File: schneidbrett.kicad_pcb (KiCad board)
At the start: 4 copper layers, 129 parts, among them J1 USB_C_Receptacle, J2 Audio_Jack_Input, J3 Audio_Jack_Output, J4 UART_CONNECTOR, J6 I2C_CONNECTOR, J7 ST-LINK_V2_20Pin_Connector, U1 MAX604CSA, U2 AD9833xRM, U3 STM32F767ZITx, U4 LM4881M, U5 FT230XQ, Y1 25MHz

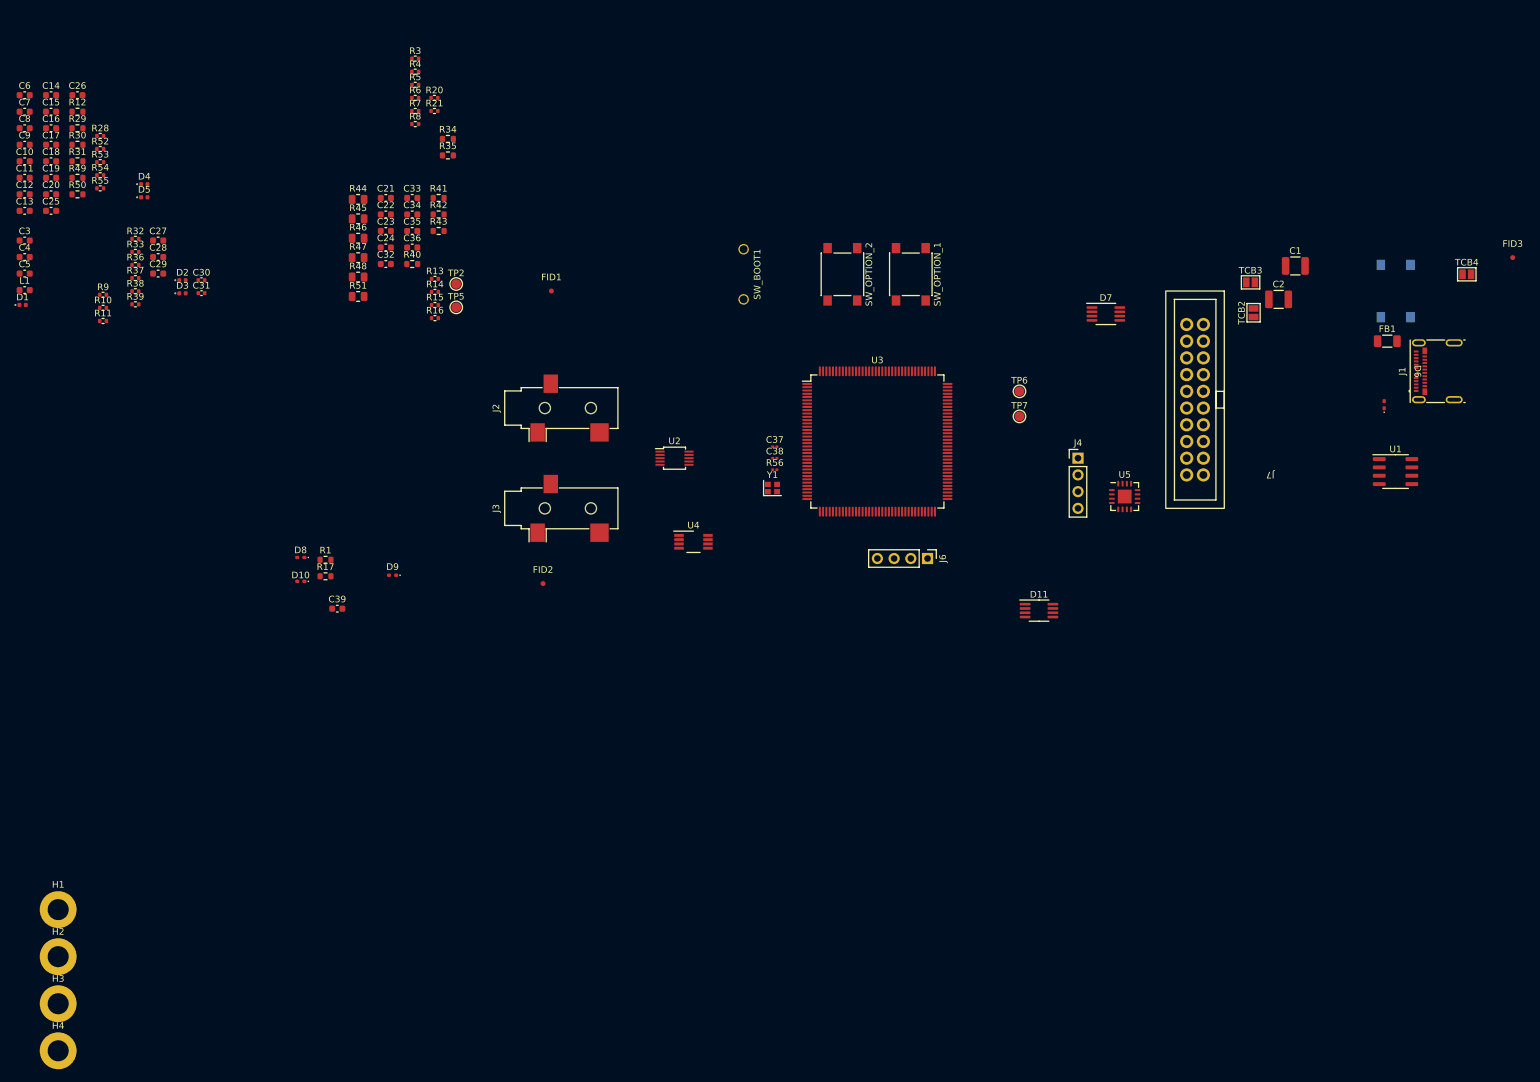
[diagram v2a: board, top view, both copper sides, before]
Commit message: Layout done, footprints mostly assigned, 3D models assigned if not annoying to get. Few TODOs left and they are marked on the PCB.
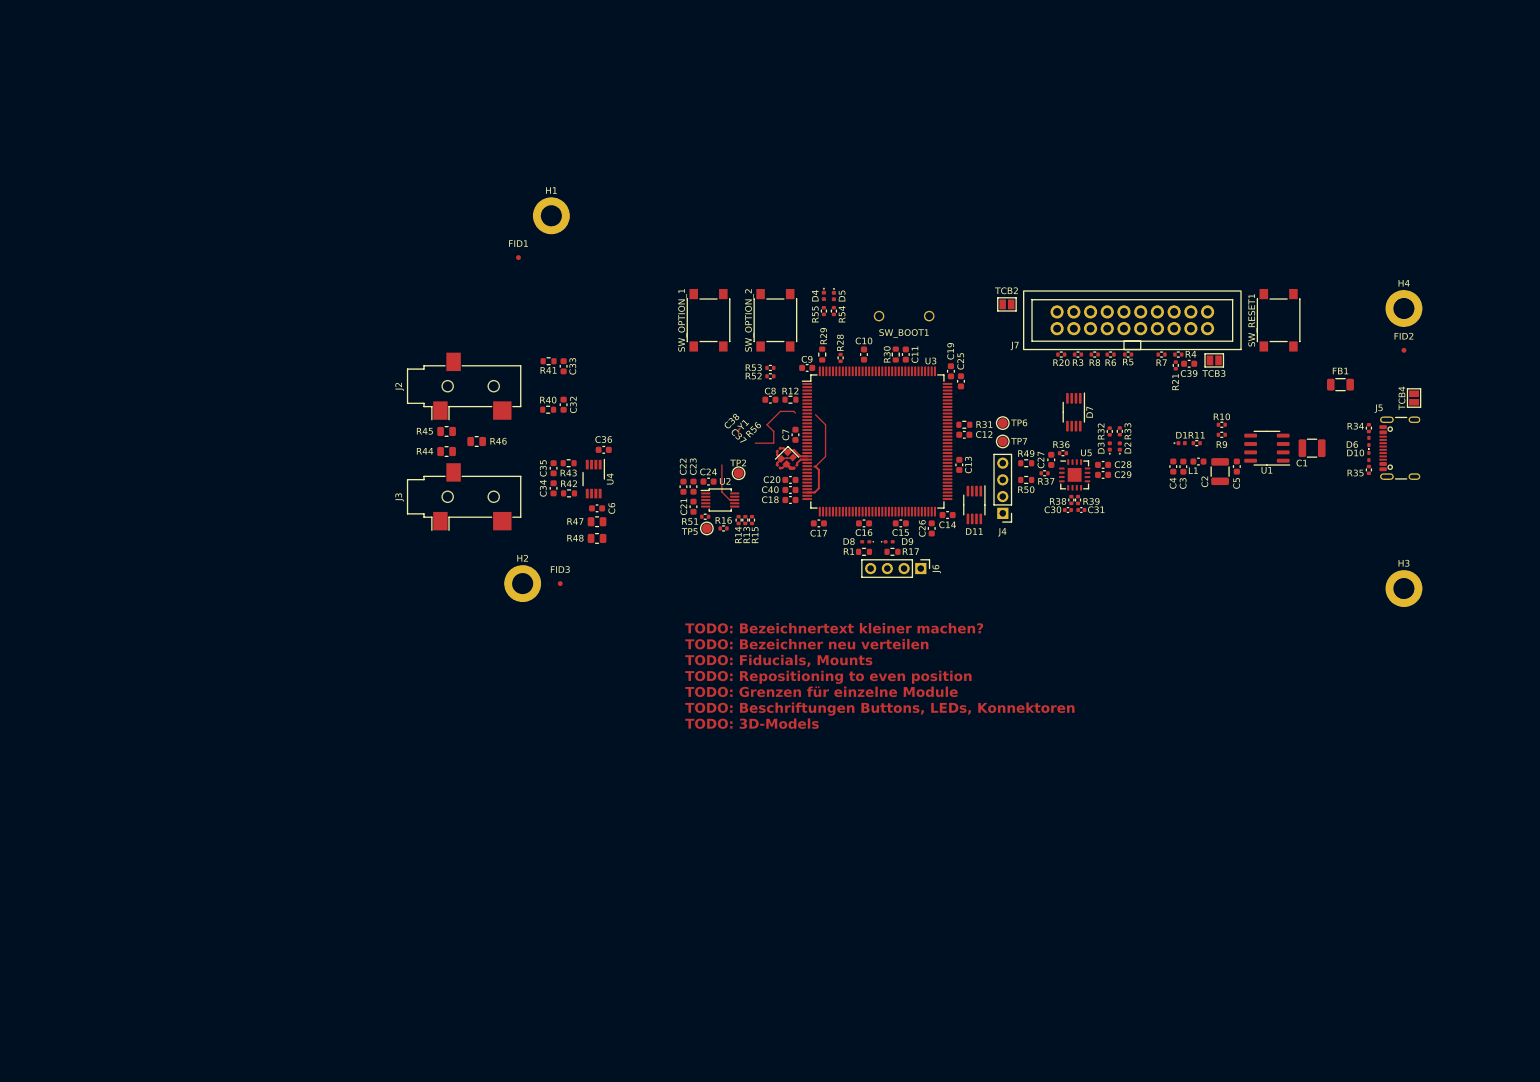
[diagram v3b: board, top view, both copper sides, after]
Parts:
- removed J1: USB_C_Receptacle, Connector_USB:USB_C_Receptacle_Molex_105450-0101
- added C40: 100n, Capacitor_SMD:C_0603_1608Metric, F.Cu at (134.1, 101.3)
- added J5: USB_C_Receptacle_USB2.0, Connector_USB:USB_C_Receptacle_GCT_USB4105-xx-A_16P_TopMnt_Horizontal, F.Cu at (227.8, 95.0)
- C18: value 100n -> 1u
- C6: value 10u -> 100n
- R34, R35: footprint Resistor_SMD:R_0603_1608Metric -> Resistor_SMD:R_0402_1005Metric
- R51: footprint Resistor_SMD:R_0805_2012Metric -> Resistor_SMD:R_0402_1005Metric
- SW_RESET1: moved to F.Cu
- moved H4 233.5 mm to (227.3, 73.8)
- moved H3 214.0 mm to (227.3, 116.3)
- moved C5 186.5 mm to (201.9, 97.8), turned to -90 degrees
- moved L1 180.2 mm to (196.1, 97.0), turned to 180 degrees
- moved C3 179.4 mm to (193.8, 97.8), turned to -90 degrees
- moved C4 177.4 mm to (192.3, 97.8), turned to -90 degrees
- moved D1 177.3 mm to (193.5, 94.2)
- moved R9 171.3 mm to (199.6, 93.0), turned to 180 degrees
- moved R10 170.9 mm to (199.6, 91.4)
- moved R11 167.2 mm to (195.8, 94.2)
- moved D10 163.4 mm to (222.0, 96.3), turned to 90 degrees
- moved FID3 152.9 mm to (99.1, 115.6)
- moved R33 152.0 mm to (184.2, 92.4), turned to 90 degrees
- moved R32 150.9 mm to (182.6, 92.5), turned to 90 degrees
- moved R50 150.5 mm to (169.9, 99.8)
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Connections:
- net Net-(D1-A) renamed /Power Supply/POWER_LED
- C18 pad 1: +3.3V -> +3.3VA
- C6 pad 1: +3.3V -> /Analog/AUDIO_PWR_JUNCTION
- R34 pad 1: /Connectors/USB_CC12 -> /Connectors/USB_CC2
- TCB4 pad 1: /Connectors/USB_CC1 -> /Connectors/USB_SHIELDING
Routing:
- net GEN_SPI_CSEL: track 0.00 -> 19.0 mm
- net GEN_WAVEFORM: track 0.00 -> 14.9 mm
- net MCU_CRYSTAL_PH0: track 0.00 -> 4.86 mm
- net GND: track 0.00 -> 4.61 mm
- net /Controller/MCU_CRYSTAL_3: track 0.00 -> 2.58 mm
- net MCU_CRYSTAL_PH1: track 0.00 -> 2.05 mm
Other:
- rule pad_to_mask_clearance: 0 -> 0.0762
- board text added: "TODO: Bezeichnertext kleiner machen? TODO: Bezeichner neu verteilen TODO: Fiducials, Mounts TODO: Repositioning to even position TODO: Grenzen für einzelne Module TODO: Beschriftungen Buttons, LEDs, Konnektoren TODO: 3D-Models"

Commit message: Board outline finished, component placement, added markers, added annotations, etc.
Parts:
- added D12: SML-LX0402UPGC-TR, LED_SMD:LED_0402_1005Metric, F.Cu at (214.4, 91.4)
- added J1: GPIO_CONNECTOR, Connector_PinHeader_2.54mm:PinHeader_1x04_P2.54mm_Vertical, F.Cu at (168.4, 113.3)
- added R2: 680R, Resistor_SMD:R_0402_1005Metric, F.Cu at (216.7, 91.4)
- added TP1: PWR_TP_5V, TestPoint:TestPoint_Pad_D1.5mm, F.Cu at (214.9, 100.3)
- added TP3: PWR_TP_3V3, TestPoint:TestPoint_Pad_D1.5mm, F.Cu at (198.6, 93.7)
- added TP4: PWR_TP_3V3A, TestPoint:TestPoint_Pad_D1.5mm, F.Cu at (189.0, 97.0)
- added TP8: PWR_TP_GND, TestPoint:TestPoint_Pad_D1.5mm, F.Cu at (228.6, 84.0)
- SIG OUT: renamed from TP2
- moved H1 22.6 mm to (81.3, 75.1)
- moved H2 12.5 mm to (81.3, 112.6)
- moved FID3 10.7 mm to (88.9, 112.6)
- moved FID2 10.2 mm to (218.4, 75.1)
- moved FID1 9.86 mm to (88.9, 75.1)
- moved C39 5.48 mm to (195.1, 87.6)
- moved R21 5.28 mm to (191.8, 87.6), turned to 180 degrees
- moved FB1 4.10 mm to (219.7, 88.9)
- moved H3 3.96 mm to (226.1, 112.6)
- moved R4 3.69 mm to (193.3, 84.5)
- moved R7 3.68 mm to (190.5, 84.5)
- moved R20 3.68 mm to (175.3, 84.5)
- moved R3 3.68 mm to (177.8, 84.5)
- moved R5 3.68 mm to (185.4, 84.5)
- moved R6 3.68 mm to (182.8, 84.5)
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- renumbered SW_BOOT1 to BOOT, SW_OPTION_1 to BTN1, SW_OPTION_2 to BTN2, TP6 to CTS, TP5 to MCLK, SW_RESET1 to RESET, TP7 to RTS
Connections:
- net /Power Supply/POWER_LED renamed /Power Supply/POWER_LED_3V3
- U3 pad 65: unconnected-(U3-PE12-Pad65) -> GPIO_OPT_0
- U3 pad 66: unconnected-(U3-PE13-Pad66) -> GPIO_OPT_1
- U3 pad 67: unconnected-(U3-PE14-Pad67) -> GPIO_OPT_2
- U3 pad 68: unconnected-(U3-PE15-Pad68) -> GPIO_OPT_3
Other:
- board outline added: 154.9 x 47.6 mm
- board text added: "-"
- board text added: "3V3"
- board text added: "3V3A"
- board text added: "65"
- board text added: "66"
- board text added: "67"
- board text added: "68"
- board text added: "AUDIO"
- board text added: "AUDIO IN"
- board text added: "AUDIO OUT"
- board text added: "Alles klonker?"
- board text added: "CLKGEN"
- board text added: "GND"
- board text added: "GPIOs"
- board text added: "I2C"
- board text added: "JTAG"
- board text added: "LED1"
- board text added: "LED2"
- board text added: "NSRST"
- board text added: "NTRST"
- board text added: "OFF"
- board text added: "ON"
- board text added: "POWER"
- board text added: "REV A 02/24"
- board text added: "RX"
- board text added: "SCL"
- board text added: "SDA"
- board text added: "SINEGEN"
- board text added: "Schneidbrett"
- board text added: "TCK"
- board text added: "TDI"
- board text added: "TDO"
- board text added: "TMS"
- board text added: "TX"
- board text added: "Timo Vandrey"
- board text added: "UART"
- board text added: "VDD"
- board text removed: "TODO: Bezeichnertext kleiner machen? TODO: Bezeichner neu verteilen TODO: Fiducials, Mounts TODO: Repositioning to even position TODO: Grenzen für einzelne Module TODO: Beschriftungen Buttons, LEDs, Konnektoren TODO: 3D-Models"

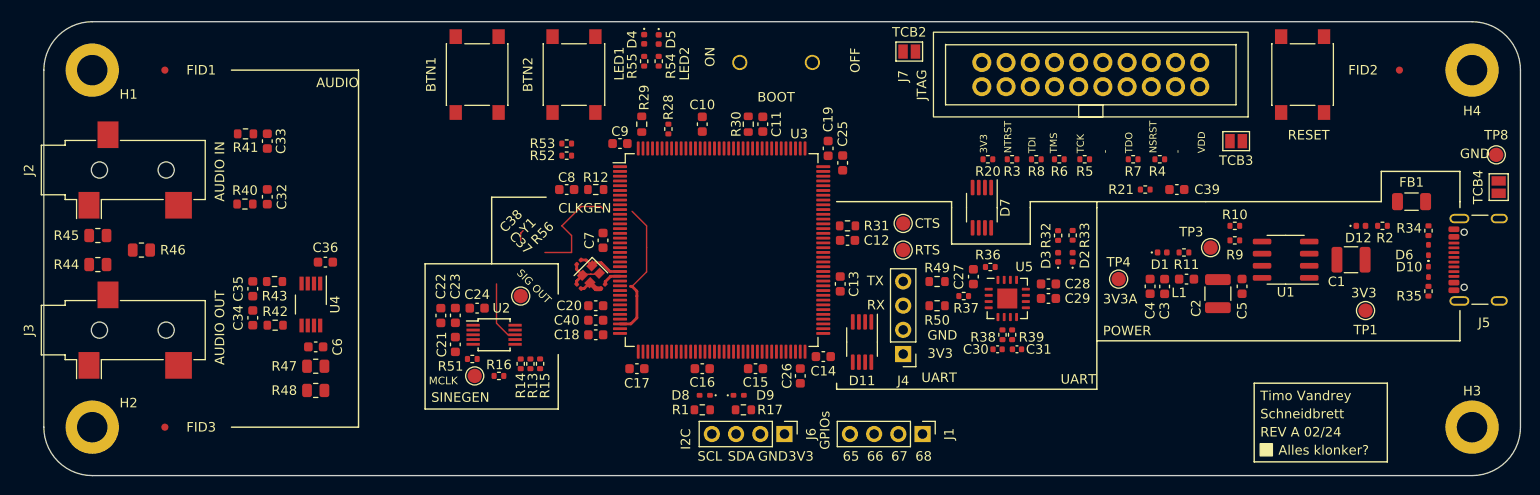
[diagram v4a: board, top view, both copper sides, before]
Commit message: Layout and routing basically done, check again before delivering
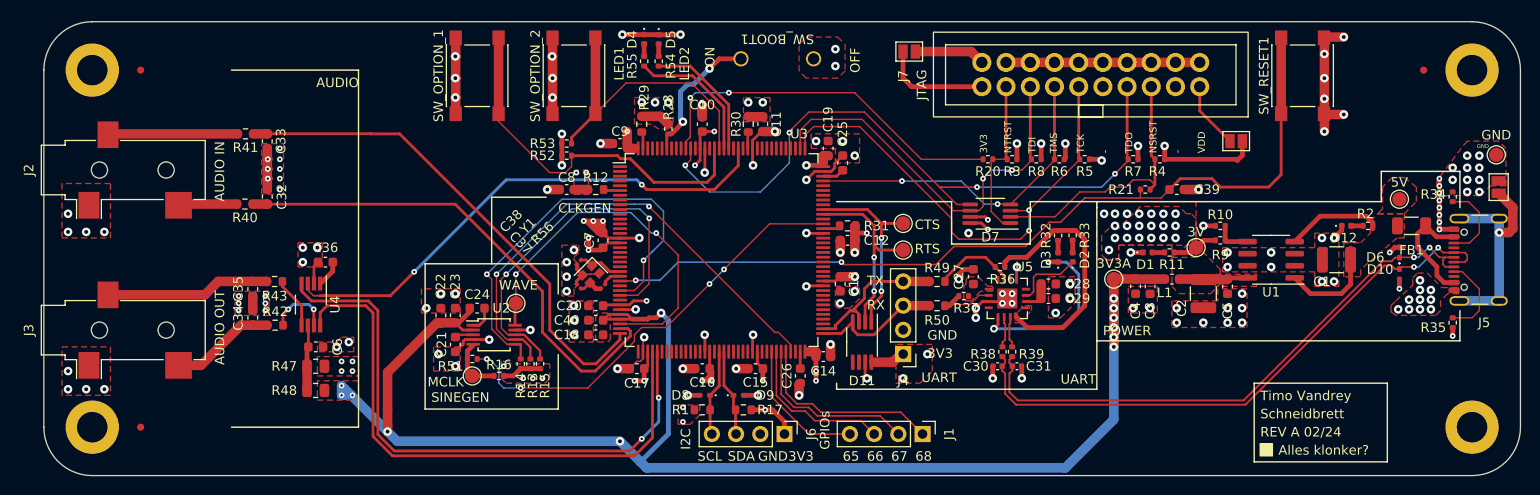
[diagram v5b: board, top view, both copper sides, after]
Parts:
- removed BOOT: SW_DIP_x01, TimosFootprints:DS01-254-L-01BE
- removed BTN1, BTN2, RESET: PTS645SM43SMTR92 LFS, Button_Switch_SMD:SW_SPST_PTS645
- removed R44, R45, R46: 0R, Resistor_SMD:R_0805_2012Metric
- removed SIG OUT: TestPoint, TestPoint:TestPoint_Pad_D1.5mm
- removed TP1: PWR_TP_5V, TestPoint:TestPoint_Pad_D1.5mm
- removed TP3: PWR_TP_3V3, TestPoint:TestPoint_Pad_D1.5mm
- removed TP4: PWR_TP_3V3A, TestPoint:TestPoint_Pad_D1.5mm
- added 3V: PWR_TP_3V3, TestPoint:TestPoint_Pad_D1.5mm, F.Cu at (197.1, 93.7)
- added 3V3A: PWR_TP_3V3A, TestPoint:TestPoint_Pad_D1.5mm, F.Cu at (188.5, 97.0)
- added 5V: PWR_TP_5V, TestPoint:TestPoint_Pad_D1.5mm, F.Cu at (218.4, 88.6)
- added SW_BOOT1: SW_DIP_x01, TimosFootprints:DS01-254-L-01BE, F.Cu at (153.2, 73.9)
- added SW_OPTION_1: PTS645SM43SMTR92 LFS, Button_Switch_SMD:SW_SPST_PTS645, F.Cu at (121.7, 75.7)
- added SW_OPTION_2: PTS645SM43SMTR92 LFS, Button_Switch_SMD:SW_SPST_PTS645, F.Cu at (131.8, 75.7)
- added SW_RESET1: PTS645SM43SMTR92 LFS, Button_Switch_SMD:SW_SPST_PTS645, F.Cu at (208.3, 75.7)
- added WAVE: TestPoint, TestPoint:TestPoint_Pad_D1.5mm, F.Cu at (125.7, 99.6)
- moved R34 4.37 mm to (224.0, 88.4)
- moved R35 4.17 mm to (224.0, 101.6)
- moved D10 3.06 mm to (218.4, 96.5)
- moved D6 3.06 mm to (218.4, 94.2)
- moved FID1 2.54 mm to (86.4, 75.1)
- moved FID3 2.54 mm to (86.4, 112.6)
- moved FB1 2.54 mm to (219.7, 91.4)
- moved FID2 2.54 mm to (221.0, 75.1)
- moved C30 1.78 mm to (176.3, 106.2)
- moved C31 1.78 mm to (178.3, 106.2)
- moved R38 1.78 mm to (176.8, 104.6)
- moved R39 1.78 mm to (177.8, 104.6)
- moved C1 1.52 mm to (211.8, 95.0)
- moved C3 1.52 mm to (192.3, 97.8)
- moved C4 1.52 mm to (190.8, 97.8)
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- renumbered TP8 to GND
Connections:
- C32 pad 2: Audio_In_GND -> GND
- C33 pad 2: Audio_In_GND -> GND
- C34 pad 2: Audio_Out_GND -> GND
- C35 pad 2: Audio_Out_GND -> GND
- D12 pad 1: unconnected-(D12-K-Pad1) -> GND
- J2 pad S: Audio_In_GND -> GND
- J3 pad S: Audio_Out_GND -> GND
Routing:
- net +3.3VA: track 0.00 -> 161.7 mm, vias 0 -> 12
- net GND: track 4.61 -> 149.1 mm, vias 0 -> 151
- net +3.3V: track 0.00 -> 123.5 mm, vias 0 -> 70
- net JTAG_NSRST: track 0.00 -> 90.3 mm, vias 0 -> 2
- net JTAG_TDO: track 0.00 -> 71.4 mm, vias 0 -> 4
- net USB+: track 0.00 -> 62.7 mm, vias 0 -> 2
- net Audio_Out_Right_MCU: track 0.00 -> 61.5 mm, vias 0 -> 2
- net Audio_Out_Left_MCU: track 0.00 -> 60.5 mm
- net USB-: track 0.00 -> 60.3 mm, vias 0 -> 2
- net Audio_Shutdown: track 0.00 -> 55.0 mm, vias 0 -> 2
- net Audio_In_Right_Filtered: track 0.00 -> 53.0 mm
- net Audio_In_Left_Filtered: track 0.00 -> 52.6 mm
- net GEN_SPI_CLK: track 0.00 -> 52.1 mm, vias 0 -> 2
- net JTAG_TCK: track 0.00 -> 50.7 mm, vias 0 -> 2
- net GEN_REFCLK: track 0.00 -> 46.0 mm, vias 0 -> 4
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- added copper zone on F.Cu, net +3.3V
- added copper zone on In2.Cu, net +3.3V
- added copper zone on F.Cu, net +3.3VA
- added copper zone on F.Cu, net +5V
- added copper zone on F.Cu, net +VCCIO_FTDI
- added copper zone on F.Cu, net GND
- added copper zone on In1.Cu, net GND
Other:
- board text removed: "3V3A"

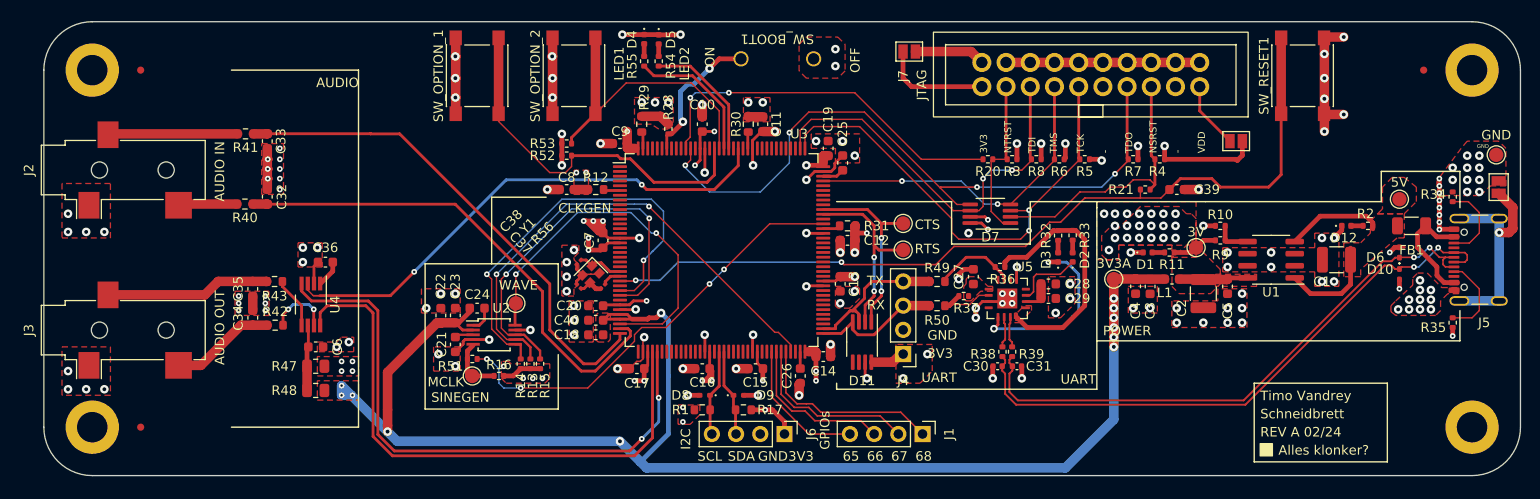
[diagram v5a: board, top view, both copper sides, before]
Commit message: Routing, Zone fillings, stitching vias, etc.
- Routing is now done, unconnected pads are connected now
- Ground pour on top and bottom layer; other zones were changed for
  compliance
- Other routing and connections
- Stitching vias
- Other minor changes
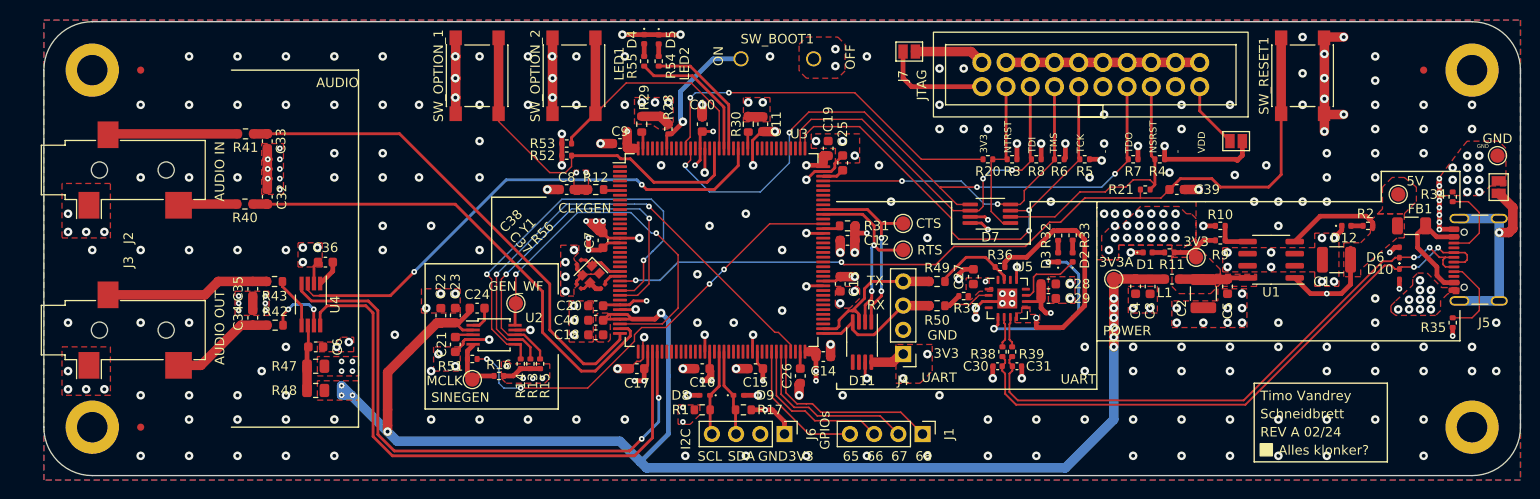
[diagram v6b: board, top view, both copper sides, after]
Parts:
- removed 3V: PWR_TP_3V3, TestPoint:TestPoint_Pad_D1.5mm
- removed WAVE: TestPoint, TestPoint:TestPoint_Pad_D1.5mm
- added 3V3: PWR_TP_3V3, TestPoint:TestPoint_Pad_D1.5mm, F.Cu at (197.1, 94.7)
- added GEN_WF: TestPoint, TestPoint:TestPoint_Pad_D1.5mm, F.Cu at (125.7, 99.6)
- moved 5V 0.52 mm to (218.3, 88.1)
- moved MCLK 0.38 mm to (121.2, 107.6)
- moved GND 0.15 mm to (228.7, 84.1)
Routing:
- net +5V: track 24.2 -> 61.3 mm, vias 0 -> 2
- net +VCCIO_FTDI: track 26.2 -> 33.3 mm, vias 0 -> 2
- net GND: track 149.1 -> 148.4 mm, vias 151 -> 311
- net JTAG_TMS: track 34.9 -> 35.5 mm
- net +3.3V: track 123.5 -> 123.4 mm, vias 70 -> 69
- net /Controller/MCU_BOOT0: vias 2 -> 1
- net +3.3VA: vias 12 -> 11
- added copper zone on B.Cu, net GND
